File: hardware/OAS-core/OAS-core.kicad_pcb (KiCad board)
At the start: 2 copper layers, 21 parts, among them J4 XT30PW-M, U1 ESP32-WROOM-32, U2 TPS2116DRL, U4 TPS26600, U5 TPS563202DRLR, U6 TPS5430DDA

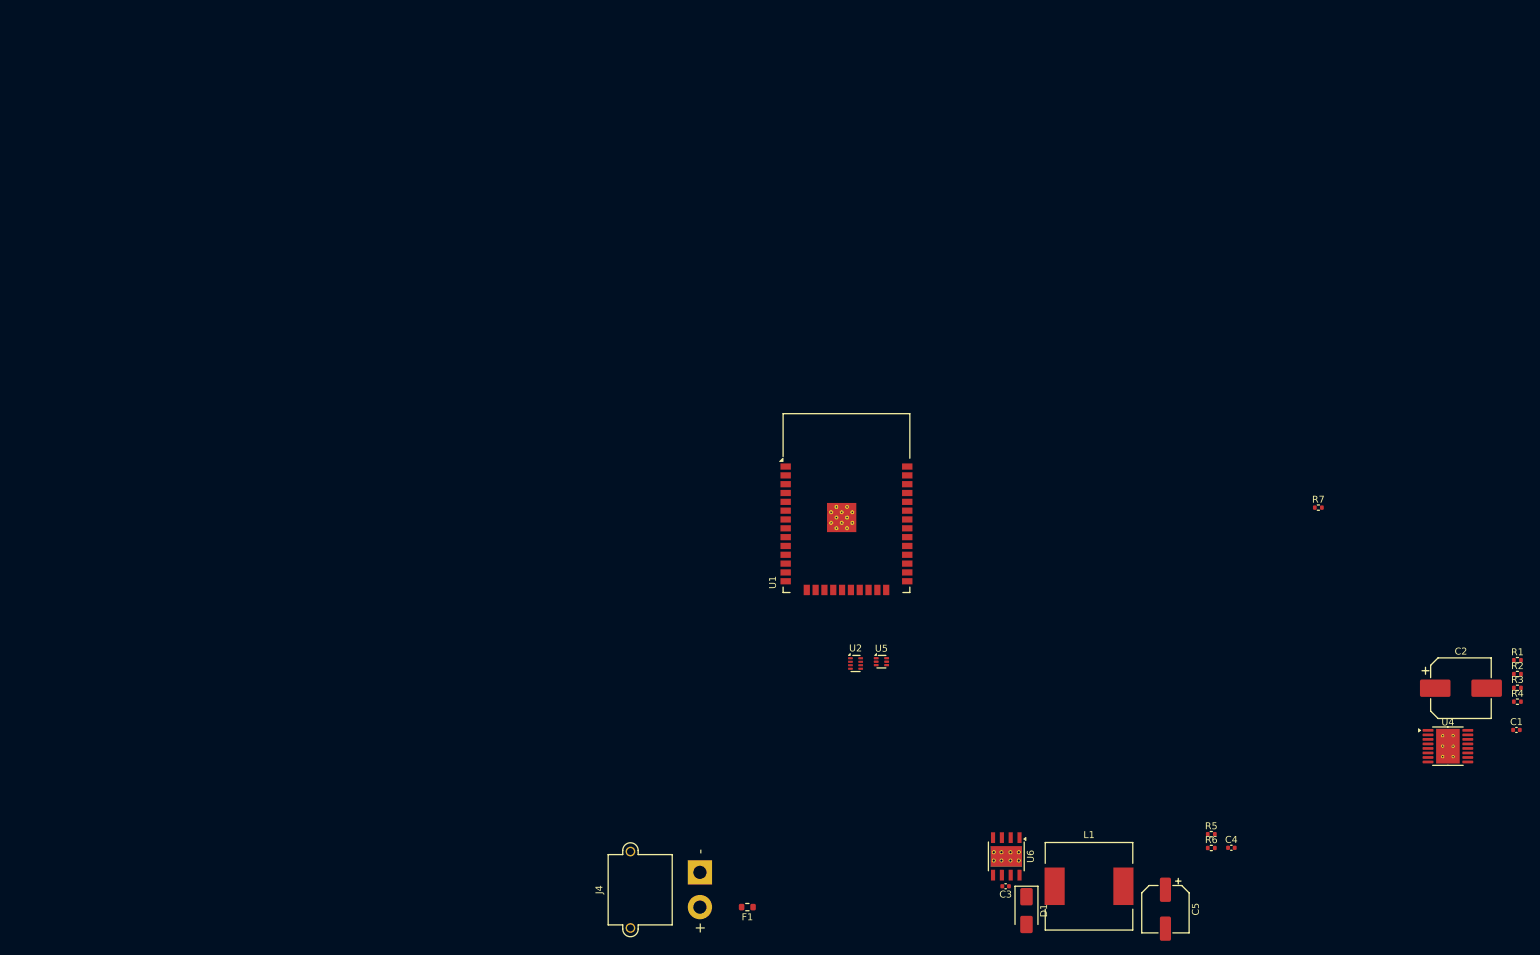
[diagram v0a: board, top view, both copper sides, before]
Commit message: MCU PSU spec + impl
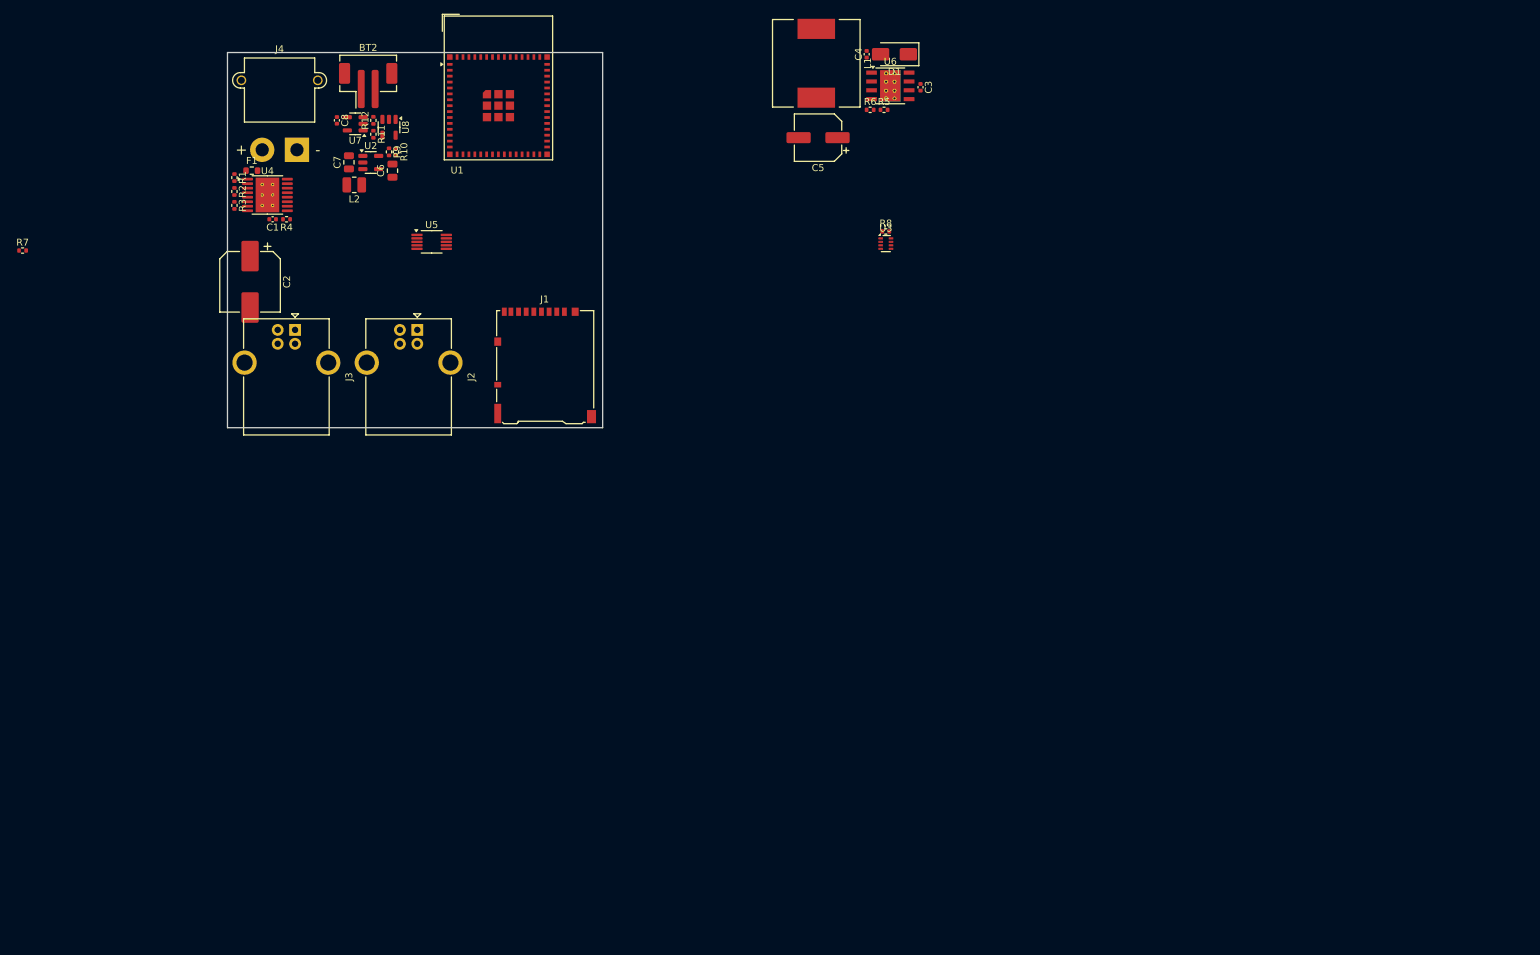
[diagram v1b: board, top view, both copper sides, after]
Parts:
- added BT2: Battery_Cell, Connector_JST:JST_PH_B2B-PH-SM4-TB_1x02-1MP_P2.00mm_Vertical, F.Cu at (20.2, 4.75)
- added C6: 10u, Capacitor_SMD:C_0805_2012Metric, F.Cu at (23.8, 17.0)
- added C7: 10u, Capacitor_SMD:C_0805_2012Metric, F.Cu at (17.5, 15.8)
- added C8: 1u, Capacitor_SMD:C_0402_1005Metric, F.Cu at (15.8, 9.76)
- added J1: Micro_SD_Card, Connector_Card:microSD_HC_Hirose_DM3AT-SF-PEJM5, F.Cu at (45.7, 45.0)
- added J2: PROG, Connector_USB:USB_B_OST_USB-B1HSxx_Horizontal, F.Cu at (27.3, 39.9)
- added J3: MSC, Connector_USB:USB_B_OST_USB-B1HSxx_Horizontal, F.Cu at (9.73, 39.9)
- added L2: 2.2u, Inductor_SMD:L_1008_2520Metric, F.Cu at (18.2, 19.1)
- added R10: 47K, Resistor_SMD:R_0402_1005Metric, F.Cu at (24.2, 14.3)
- added R11: 10k, Resistor_SMD:R_0402_1005Metric, F.Cu at (21.0, 11.8)
- added R12: 100, Resistor_SMD:R_0402_1005Metric, F.Cu at (21.0, 9.76)
- added R8: 47K, Resistor_SMD:R_0402_1005Metric, F.Cu at (94.8, 25.8)
- added R9: 47K, Resistor_SMD:R_0402_1005Metric, F.Cu at (23.2, 14.3)
- added U3: LM66200, Package_TO_SOT_SMD:SOT-583-8, F.Cu at (94.8, 27.5)
- added U7: TP4054, Package_TO_SOT_SMD:TSOT-23-5, F.Cu at (18.4, 10.3)
- added U8: DW02, Package_TO_SOT_SMD:SOT-23-5, F.Cu at (23.2, 10.8)
- U1: value ESP32-WROOM-32 -> ESP32-S3-MINI-1; footprint RF_Module:ESP32-WROOM-32 -> RF_Module:ESP32-S2-MINI-1
- U2: value TPS2116DRL -> MT3406; footprint Package_TO_SOT_SMD:SOT-583-8 -> Package_TO_SOT_SMD:SOT-23-5
- U5: value TPS563202DRLR -> CH340X; footprint Package_TO_SOT_SMD:SOT-563 -> Package_SO:MSOP-10_3x3mm_P0.5mm
- moved R1 197.3 mm to (1.00, 18.0), turned to -90 degrees
- moved R2 197.3 mm to (1.00, 20.0), turned to -90 degrees
- moved R3 197.3 mm to (1.00, 22.0), turned to -90 degrees
- moved C1 193.5 mm to (6.50, 24.0), turned to 180 degrees
- moved R4 190.3 mm to (8.50, 24.0), turned to 180 degrees
- moved R7 190.1 mm to (-29.5, 28.5)
- moved U4 187.5 mm to (5.75, 20.5)
- moved C2 183.8 mm to (3.25, 33.0), turned to -90 degrees
- moved F1 127.8 mm to (3.50, 17.0), turned to 0 degrees
- moved C4 125.7 mm to (92.0, 0.25), turned to 90 degrees
- moved L1 124.8 mm to (84.8, 1.55), turned to -90 degrees
- moved D1 124.7 mm to (96.0, 0.25), turned to 180 degrees
- moved C5 121.8 mm to (85.0, 12.2), turned to 180 degrees
- moved J4 119.1 mm to (10.0, 14.0), turned to 0 degrees
- moved R6 117.0 mm to (92.5, 8.25)
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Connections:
- net +5_{VIN} renamed +5V
- net +VIN_{PROT} renamed Net-(C2-Pad1)
- net Net-(U4-PAD) renamed /RTN
- U1 pad 1: Net-(U1-GND-Pad1) -> GND
- U1 pad 15: Net-(U1-GND-Pad1) -> unconnected-(U1-IO11-Pad15)
- U1 pad 2: unconnected-(U1-VDD-Pad2) -> GND
- U1 pad 38: Net-(U1-GND-Pad1) -> unconnected-(U1-IO42-Pad38)
- U1 pad 39: Net-(U1-GND-Pad1) -> unconnected-(U1-TXD0-Pad39)
- U2 pad 1: unconnected-(U2-GND-Pad1) -> Net-(U2-EN)
- U2 pad 2: Net-(U2-VOUT-Pad2) -> GND
- U2 pad 3: unconnected-(U2-VIN1-Pad3) -> Net-(U2-SW)
- U2 pad 4: unconnected-(U2-PR1-Pad4) -> Net-(U2-EN)
- U2 pad 5: unconnected-(U2-MODE-Pad5) -> Net-(U2-FB)
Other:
- board outline added: 54 x 54 mm
